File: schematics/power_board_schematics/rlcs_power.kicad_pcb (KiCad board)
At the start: 2 copper layers, 53.3 x 101.6 mm, 55 parts, among them J1 SD_Card, J10 Conn_14_to_21, J11 conn_power, J12 conn_A8_to_A15, J13 conn_A0_to_A7, J14 conn_22_to_53, J2 Conn_01x05_Male, J3 Conn_01x05_Male, J4 Battery Conn, J5 CONN_01X02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

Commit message: UPdated pcb
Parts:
- moved J4 68.9 mm to (101.6, 71.1)
- moved J7 31.8 mm to (141.0, 156.2)
- moved R14 21.7 mm to (135.6, 95.2), turned to 0 degrees
- moved R13 18.9 mm to (135.6, 92.7), turned to 180 degrees
- moved TP2 16.6 mm to (142.2, 121.9)
- moved R12 16.3 mm to (135.6, 90.2), turned to 180 degrees
- moved JP1 15.3 mm to (116.8, 146.1)
- moved R4 14.8 mm to (141.0, 105.4)
- moved R8 14.5 mm to (135.9, 87.6), turned to 180 degrees
- moved R9 12.7 mm to (135.6, 85.1), turned to 180 degrees
- moved F1 10.2 mm to (101.6, 135.9)
- moved TP3 10.2 mm to (133.3, 80.0)
- moved R2 9.92 mm to (125.7, 130.8)
- moved R1 9.16 mm to (121.9, 130.8)
- moved T1 9.16 mm to (105.4, 108.0)
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
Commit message: Updated pcb
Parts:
- moved J4 83.5 mm to (120.7, 152.4)
- moved R7 70.7 mm to (120.7, 137.2), turned to 180 degrees
- moved JP1 70.0 mm to (111.8, 76.2)
- moved R11 63.9 mm to (116.8, 137.2), turned to 180 degrees
- moved R10 62.3 mm to (124.5, 137.2), turned to 180 degrees
- moved R2 50.6 mm to (115.6, 81.3), turned to 90 degrees
- moved R1 49.7 mm to (118.1, 81.3)
- moved R1 49.6 mm to (120.7, 81.3)
- moved J7 48.3 mm to (101.6, 128.3), turned to 0 degrees
- moved TP2 44.2 mm to (100.3, 108.0)
- moved R16 38.2 mm to (134.6, 77.5)
- moved C2 37.4 mm to (137.2, 77.5)
- moved R15 36.7 mm to (132.1, 77.5)
- moved R4 36.3 mm to (111.8, 83.8)
- moved R9 34.3 mm to (135.9, 119.4)
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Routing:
- net GND: track 0.00 -> 249.6 mm, vias 0 -> 7
- net +5V: track 0.00 -> 230.5 mm, vias 0 -> 2
- net +12V: track 0.00 -> 132.3 mm, vias 0 -> 1
- net +3V3: track 0.00 -> 81.2 mm, vias 0 -> 2
- net ARD_CON_SD_WP: track 0.00 -> 38.1 mm, vias 0 -> 1
- net Net-(AFF1-Pad7): track 0.00 -> 33.0 mm
- net Net-(J11-Pad6): track 0.00 -> 31.0 mm
- net Net-(J1-Pad1): track 0.00 -> 29.2 mm, vias 0 -> 2
- net Net-(J1-Pad8): track 0.00 -> 22.0 mm, vias 0 -> 1
- net Net-(AFF1-Pad10): track 0.00 -> 21.9 mm, vias 0 -> 1
- net ARD_CON_SD_CD: track 0.00 -> 21.4 mm, vias 0 -> 1
- net Net-(AFF1-Pad2): track 0.00 -> 20.3 mm
- net Net-(AFF1-Pad3): track 0.00 -> 17.9 mm
- net Net-(AFF1-Pad4): track 0.00 -> 16.3 mm, vias 0 -> 1
- net Net-(J1-Pad5): track 0.00 -> 15.9 mm, vias 0 -> 2
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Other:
- board size 53.3 x 101.6 mm -> 55.9 x 106.7 mm
- board text removed: "3v3"
- board text removed: "5v"
- board text removed: "Arduino"

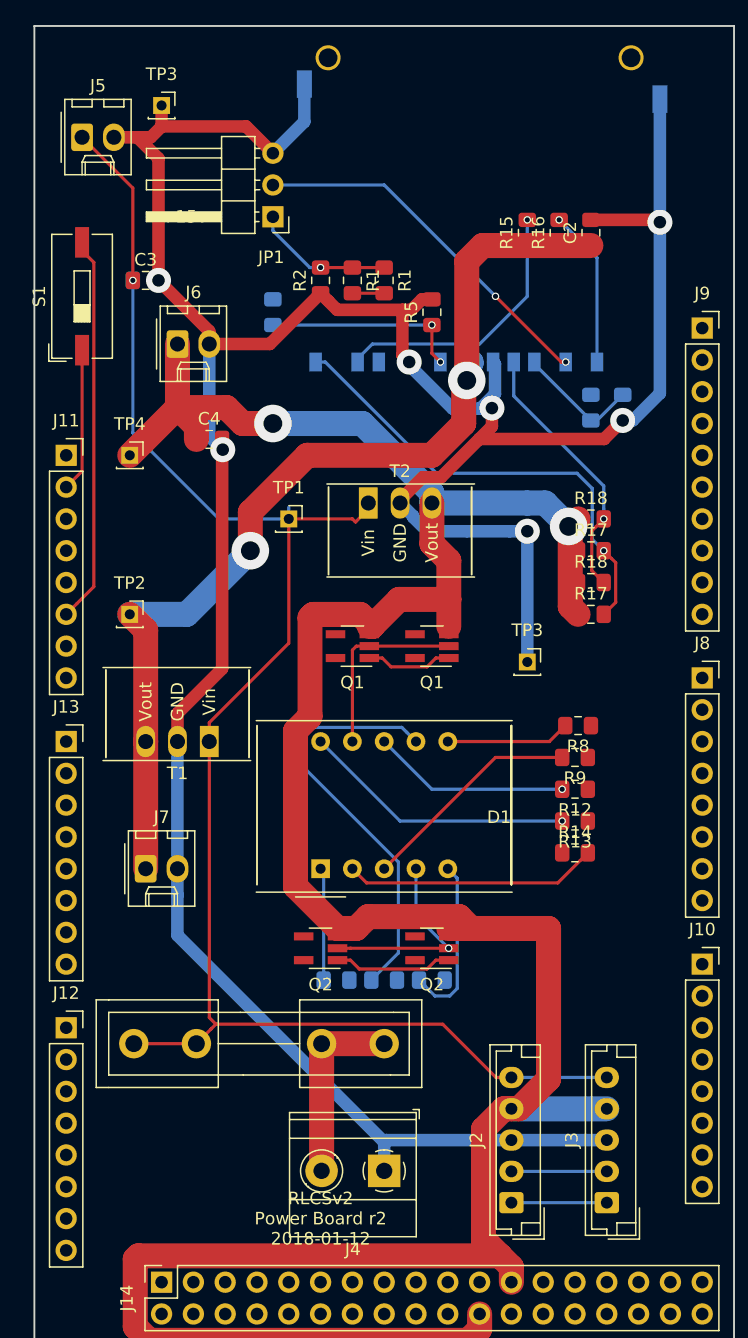
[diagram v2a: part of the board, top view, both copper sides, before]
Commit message: Updated PCB, still need to edit traces
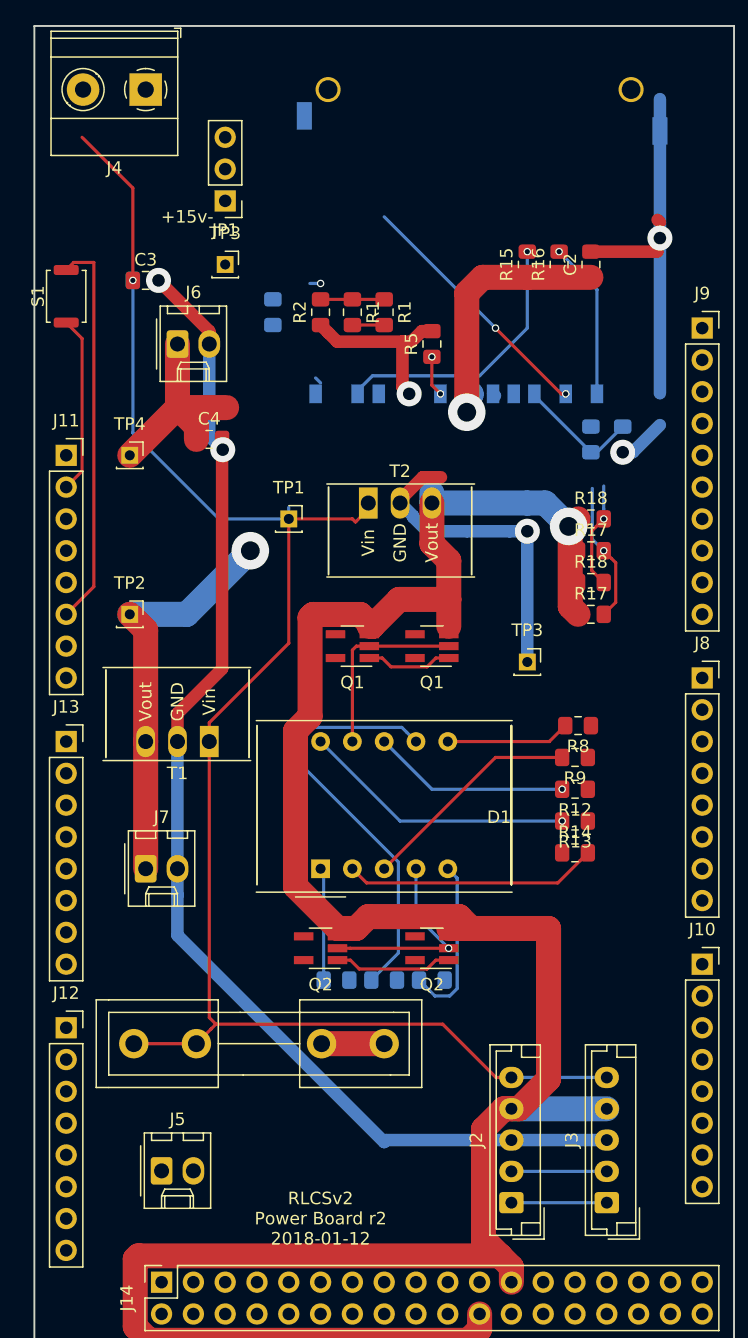
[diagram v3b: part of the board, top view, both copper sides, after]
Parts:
- JP1: footprint Connector_PinHeader_2.54mm:PinHeader_1x03_P2.54mm_Horizontal -> Connector_PinHeader_2.54mm:PinHeader_1x03_P2.54mm_Vertical
- S1: footprint Button_Switch_SMD:SW_DIP_SPSTx01_Slide_9.78x4.72mm_W8.61mm_P2.54mm -> Button_Switch_SMD:SW_Push_SPST_NO_Alps_SKRK
- moved J4 88.4 mm to (101.6, 66.0)
- moved J5 82.8 mm to (102.9, 152.4)
- moved TP3 13.7 mm to (108.0, 80.0)
- moved JP1 4.02 mm to (108.0, 74.9)
- moved C2 2.54 mm to (137.2, 80.0)
- moved J1 2.54 mm to (128.3, 90.3)
- moved R15 2.54 mm to (132.1, 80.0)
- moved R16 2.54 mm to (134.6, 80.0)
- moved R3 2.54 mm to (137.2, 94.0)
- moved R5 2.54 mm to (124.5, 86.4)
- moved R6 2.54 mm to (139.7, 94.0)
- moved R1 2.54 mm to (118.1, 83.8)
- moved R1 2.54 mm to (120.7, 83.8)
- moved R2 2.54 mm to (115.6, 83.8)
- moved S1 1.27 mm to (95.2, 82.5)
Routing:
- net GND: track 249.6 -> 172.0 mm, vias 7 -> 6
- net +3V3: track 81.2 -> 54.5 mm
- net ARD_CON_SD_WP: track 38.1 -> 11.8 mm
- net +5V: track 230.5 -> 211.3 mm, vias 2 -> 1
- net ARD_CON_SD_CD: track 21.4 -> 8.50 mm
- net Net-(J1-Pad5): track 15.9 -> 3.24 mm
- net Net-(F1-Pad1): track 15.2 -> 5.00 mm
- net Net-(J1-Pad1): track 29.2 -> 20.4 mm
- net Net-(JP1-Pad1): track 11.2 -> 5.94 mm
- net Net-(J11-Pad2): track 11.5 -> 14.2 mm

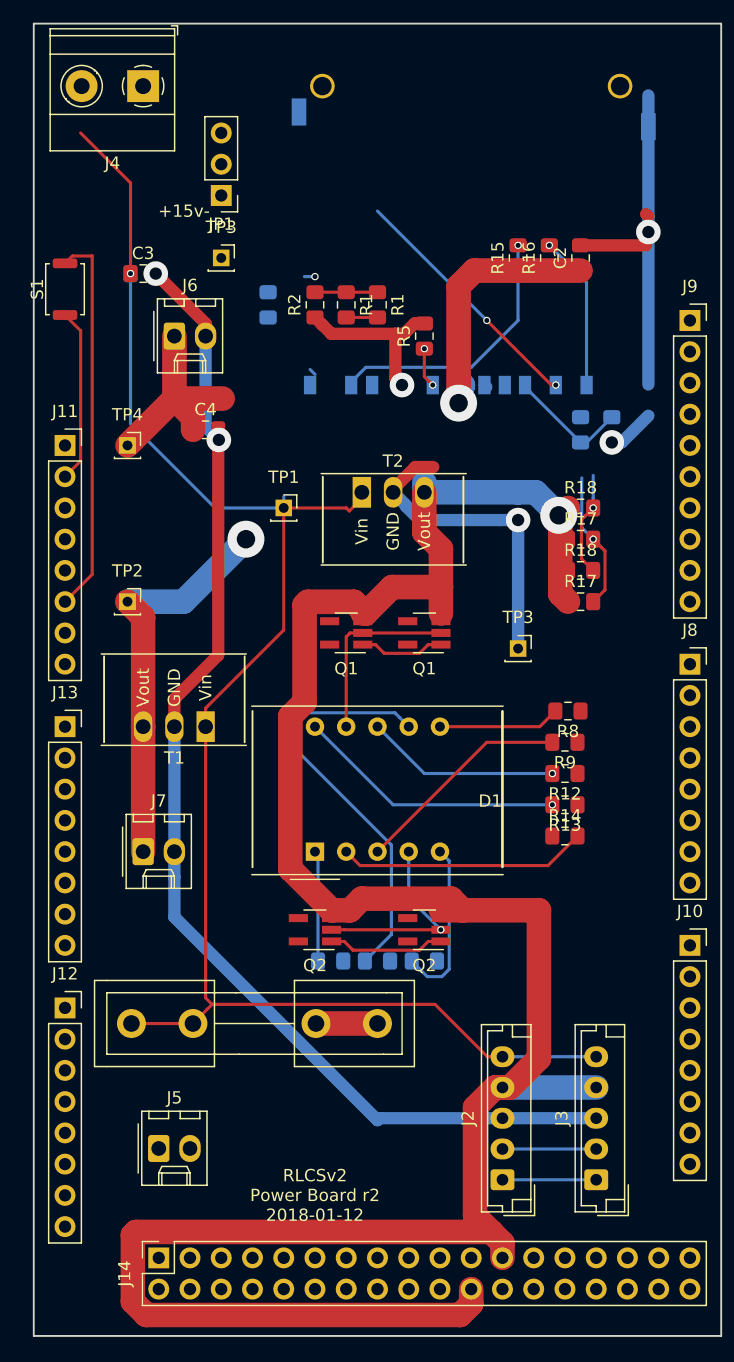
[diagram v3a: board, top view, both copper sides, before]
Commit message: dded non-power and non-ground traces
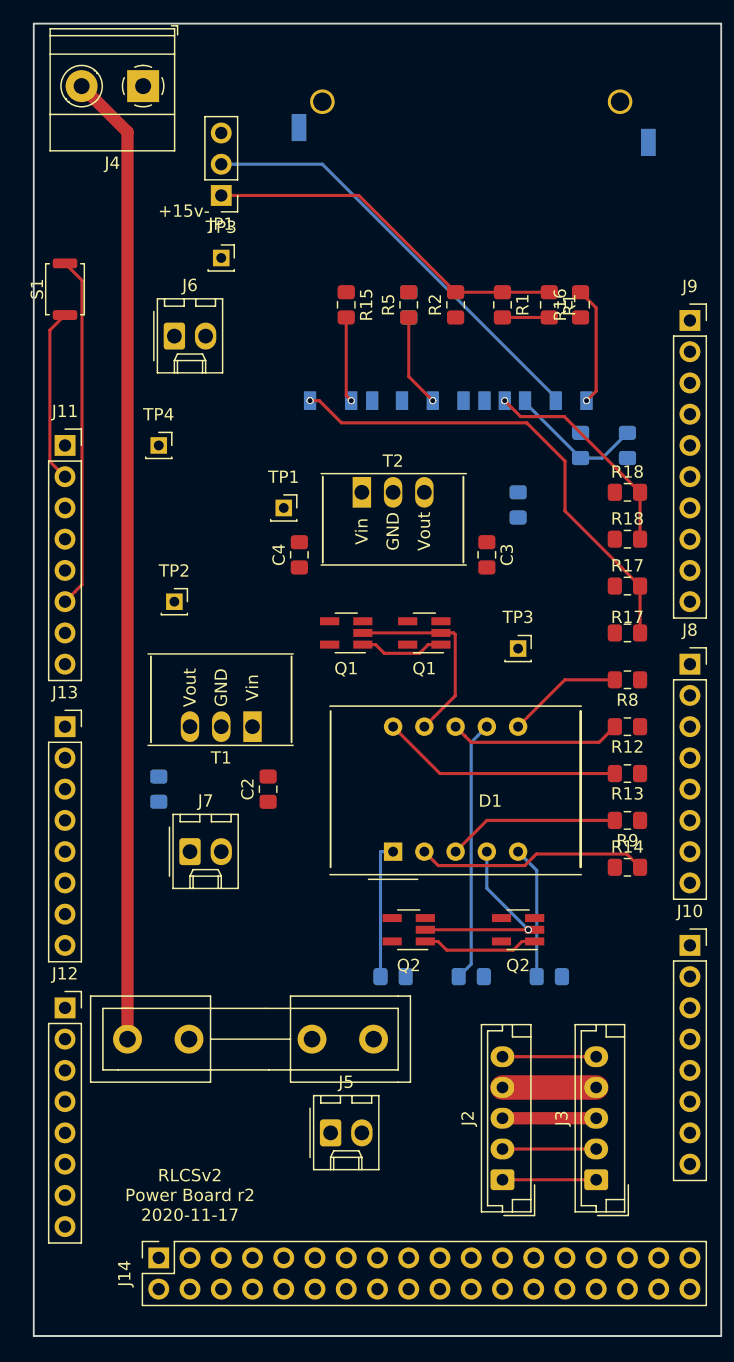
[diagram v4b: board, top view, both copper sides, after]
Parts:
- moved C2 50.1 mm to (111.8, 123.2)
- moved C1 41.9 mm to (102.9, 123.2), turned to 90 degrees
- moved C3 36.1 mm to (129.5, 104.1), turned to 270 degrees
- moved F1 20.4 mm to (100.3, 143.5), turned to 0 degrees
- moved R15 14.5 mm to (118.1, 83.8), turned to 270 degrees
- moved J5 14.0 mm to (116.8, 151.1)
- moved R1 14.0 mm to (134.6, 83.8)
- moved R1 12.7 mm to (130.8, 83.8)
- moved C4 12.7 mm to (114.3, 104.1), turned to 90 degrees
- moved R2 11.4 mm to (127.0, 83.8)
- moved R4 11.4 mm to (123.2, 83.8)
- moved R10 10.2 mm to (134.6, 138.4)
- moved R9 8.13 mm to (141.0, 125.7)
- moved R7 7.73 mm to (128.3, 138.4)
- moved Q2 7.62 mm to (132.1, 134.6)
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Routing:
- net +5V: track 211.3 -> 7.62 mm, vias 1 -> 0
- net GND: track 172.0 -> 7.62 mm, vias 6 -> 0
- net +12V: track 132.3 -> 7.62 mm, vias 1 -> 0
- net Net-(F1-Pad1): track 5.00 -> 79.0 mm
- net +3V3: track 54.5 -> 0.00 mm, vias 2 -> 0
- net ARD_CON_SD_WP: track 11.8 -> 39.3 mm
- net Net-(JP1-Pad1): track 5.94 -> 29.9 mm, vias 1 -> 0
- net Net-(J1-Pad8): track 22.0 -> 6.93 mm
- net Net-(J1-Pad1): track 20.4 -> 35.3 mm, vias 2 -> 0
- net Net-(AFF1-Pad7): track 33.0 -> 21.3 mm
- net ARD_CON_SD_CD: track 8.50 -> 17.9 mm
- net Net-(J1-Pad5): track 3.24 -> 7.57 mm, vias 2 -> 1
- net Net-(AFF1-Pad3): track 17.9 -> 14.0 mm
- net Net-(J1-Pad9): track 12.6 -> 9.67 mm
- net Net-(AFF1-Pad5): track 13.7 -> 10.8 mm
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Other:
- board text added: "RLCSv2 Power Board r2 2020-11-17"
- board text removed: "RLCSv2 Power Board r2 2018-01-12"

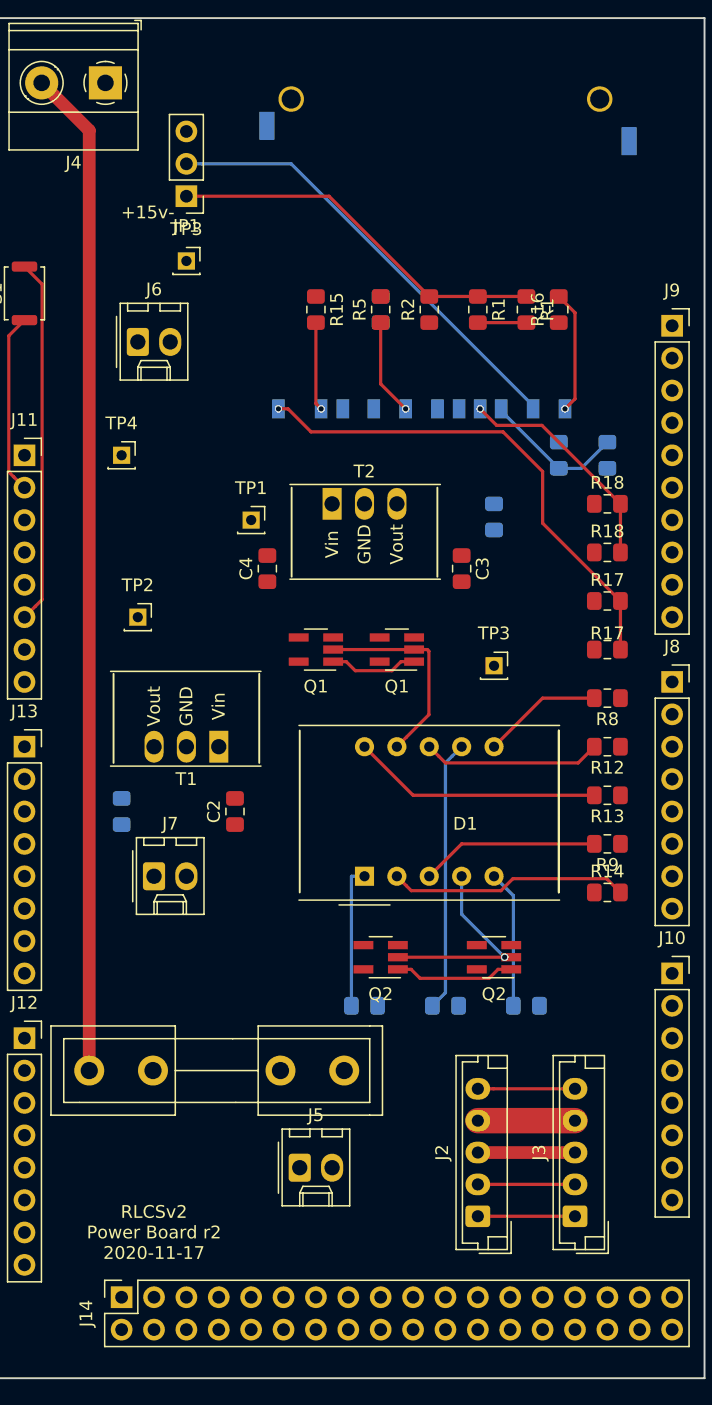
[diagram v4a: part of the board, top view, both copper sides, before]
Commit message: Added traces fro ground and power
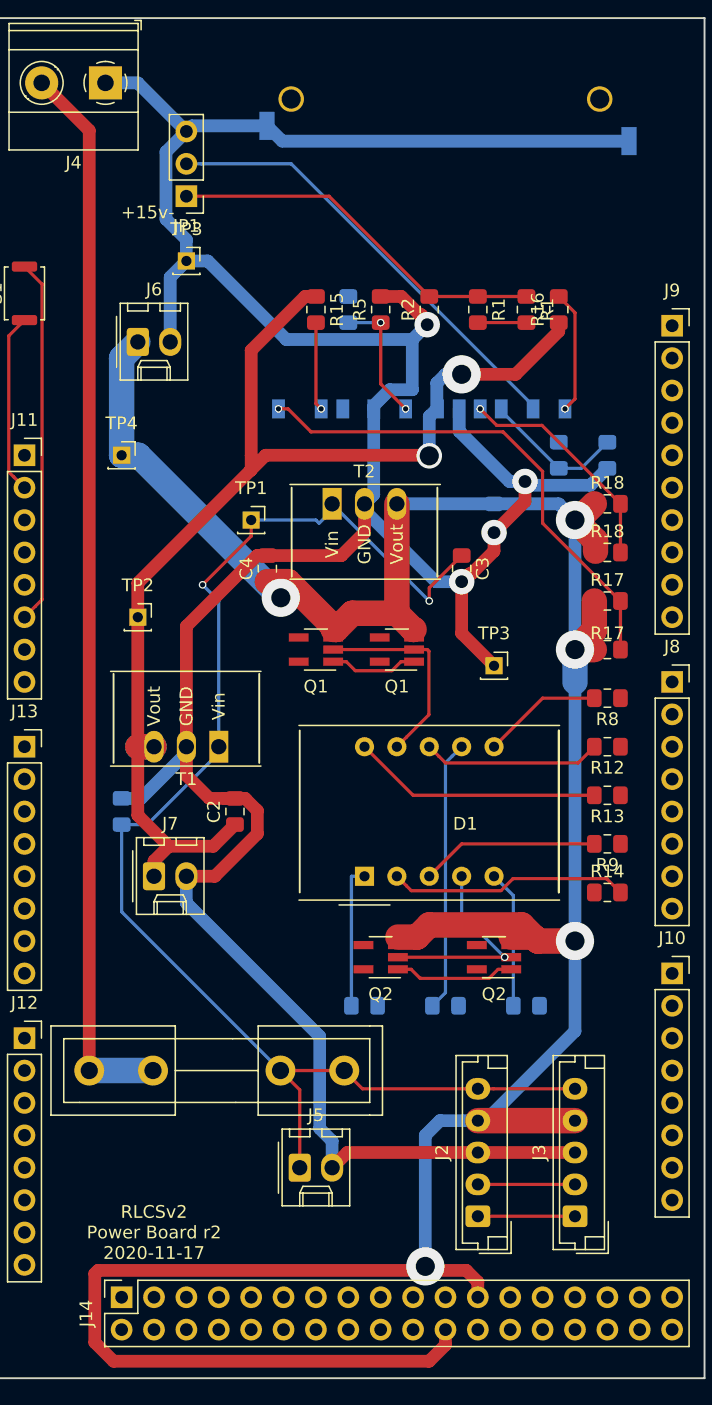
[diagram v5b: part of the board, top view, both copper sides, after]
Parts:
- moved R4 2.54 mm to (120.7, 83.8)
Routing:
- net GND: track 7.62 -> 248.1 mm, vias 0 -> 4
- net +5V: track 7.62 -> 234.7 mm, vias 0 -> 5
- net +12V: track 7.62 -> 109.5 mm, vias 0 -> 2
- net +3V3: track 0.00 -> 94.1 mm, vias 0 -> 2
- net Net-(F1-Pad1): track 79.0 -> 84.0 mm
- net Net-(J1-Pad5): track 7.57 -> 10.1 mm, vias 1 -> 2

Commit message: Address circuit review comments
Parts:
- removed the Q1 at (118.1, 110.5)
- removed the Q2 at (123.2, 134.6)
- removed the R1 at (130.8, 83.8)
- removed the R17 at (141.0, 106.7)
- removed the R18 at (141.0, 99.1)
- added G***: LOGO, rlcs:rocketry_logo_small, F.Cu at (102.9, 153.7)
- R4: moved to F.Cu
- moved J5 3.81 mm to (120.7, 151.1)
- moved R18 2.67 mm to (141.0, 105.5)
- moved R2 1.78 mm to (128.8, 83.8)
- moved R5 1.14 mm to (124.3, 83.8)
- moved R1 0.89 mm to (133.7, 83.8)
- moved R17 0.63 mm to (141.0, 109.9)
- moved R3 0.51 mm to (137.2, 95.8)
- moved R4 0.51 mm to (121.2, 83.8), turned to 270 degrees
- moved R6 0.51 mm to (141.0, 95.8)
- moved R15 0.25 mm to (117.9, 83.8)
- turned C3 to 90 degrees
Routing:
- net GND: track 248.1 -> 9.15 mm, vias 4 -> 1
- net +5V: track 234.7 -> 224.9 mm, vias 5 -> 4
- net ARD_CON_7SEG_D1: track 9.47 -> 0.00 mm
- net Net-(AFF1-Pad4): track 16.6 -> 7.75 mm
- net +12V: track 109.5 -> 114.4 mm
- net Net-(JP1-Pad1): track 29.9 -> 34.2 mm
- net ARD_CON_SD_SS: track 3.81 -> 0.00 mm
- net ARD_CON_SD_CD: track 17.9 -> 20.6 mm
- net Net-(J1-Pad5): track 10.1 -> 12.1 mm, vias 2 -> 1
- added copper zone on B.Cu, net GND
- added copper zone on F.Cu, net GND
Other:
- board text added: "CD/DAT3"
- board text added: "CLK"
- board text added: "CMD"
- board text added: "DAT0"
- board text added: "DAT1"
- board text added: "DAT2"
- board text added: "RLCSv3 Power Board r2 2021-01-17"
- board text added: "VDD"
- board text added: "VSS"
- board text removed: "RLCSv2 Power Board r2 2020-11-17"
